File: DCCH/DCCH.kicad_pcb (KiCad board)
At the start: 4 copper layers, 127 x 76.2 mm, 57 parts, among them J1 Conn_01x02, J2 Conn_01x02, J211 Conn_01x02, J212 Conn_01x02, J221 Conn_01x02, J222 Conn_01x02, J231 Conn_01x02, J232 Conn_01x02, J241 Conn_01x02, J242 Conn_01x02, J3 Conn_02x04_Odd_Even, J4 Conn_02x04_Odd_Even, U11 SN74HC595, U12 SN74HC595, U13 SN74HC595, U14 SN74HC595, U21 SN754410, U22 SN754410, U23 SN754410, U24 SN754410

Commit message: Changed orientation again.
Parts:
- moved J3 102.4 mm to (71.8, 72.4), turned to 0 degrees
- moved D2 76.4 mm to (141.3, 105.4), turned to 180 degrees
- moved R2 74.1 mm to (137.2, 105.4), turned to 180 degrees
- moved J1 64.8 mm to (113.7, 110.5), turned to 0 degrees
- moved J2 61.4 mm to (137.2, 110.5), turned to 0 degrees
- moved D1 49.7 mm to (117.8, 105.4), turned to 180 degrees
- moved R1 48.6 mm to (113.6, 105.4), turned to 180 degrees
- moved C211 41.0 mm to (102.9, 47.3)
- moved C221 41.0 mm to (123.2, 47.3)
- moved C231 41.0 mm to (143.5, 47.3)
- moved C241 41.0 mm to (163.8, 47.3)
- moved U21 41.0 mm to (92.7, 46.4)
- moved U22 41.0 mm to (113.0, 46.4)
- moved U23 41.0 mm to (133.3, 46.4)
- moved U24 41.0 mm to (153.7, 46.4)
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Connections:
- J4 pad 1: SER-14 -> GND
- J4 pad 2: GND -> SER-14
- J4 pad 3: SYNC -> GND
- J4 pad 4: GND -> SYNC
- J4 pad 5: WRITE -> GND
- J4 pad 6: GND -> WRITE
- J4 pad 7: CLEAR -> GND
- J4 pad 8: GND -> CLEAR
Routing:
- net CLEAR: track 207.6 -> 291.6 mm
- net WRITE: track 205.0 -> 285.1 mm
- net SYNC: track 202.0 -> 277.7 mm
- net CON-12G: track 25.1 -> 53.8 mm
- net CON-14G: track 25.1 -> 53.8 mm
- net CON-13G: track 25.1 -> 53.8 mm
- net CON-11G: track 25.1 -> 53.8 mm
- net CON-14E: track 47.6 -> 30.7 mm
- net CON-13E: track 47.6 -> 30.7 mm
- net CON-11E: track 47.6 -> 30.7 mm
- net CON-12E: track 47.6 -> 30.7 mm
- net CON-13D: track 46.6 -> 29.7 mm
- net CON-11D: track 46.6 -> 29.7 mm
- net CON-14D: track 46.6 -> 29.7 mm
- net CON-12D: track 46.6 -> 29.7 mm
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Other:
- rule trace_min: 0.249999 -> 0.249936
- board text added: "+24V ON"
- board text added: "+5V ON"
- board text added: "5"
- board text added: "6"
- board text added: "7"
- board text added: "8"
- board text added: "GND"
- board text removed: "+24V DC"
- board text removed: "+5V DC"
- board text removed: "A"
- board text removed: "H"
- board text removed: "Power LEDs"

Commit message: Updated silksceen as well as plots.
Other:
- board text added: "IN"
- board text added: "OUT"
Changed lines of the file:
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@@
   (general
     (thickness 1.6)
-    (drawings 78)
+    (drawings 80)
     (tracks 496)
     (zones 0)
@@
     )
   )
+  (gr_text OUT (at 180.848 82.296) (layer F.SilkS)
+    (effects (font (size 0.889 0.889) (thickness 0.1524)))
+  )
+  (gr_text IN (at 73.152 82.296) (layer F.SilkS)
+    (effects (font (size 0.889 0.889) (thickness 0.1524)))
+  )
   (gr_text 8 (at 160.02 68.58) (layer F.SilkS)
     (effects (font (size 0.889 0.889) (thickness 0.1524)))
@@
   (gr_line (start 102.235 69.85) (end 102.235 78.74) (layer F.SilkS) (width 0.12))
   (gr_line (start 91.44 69.85) (end 102.235 69.85) (layer F.SilkS) (width 0.12))
-  (gr_text "+5V ON" (at 138.684 103.505) (layer F.SilkS)
+  (gr_text "+5V ON" (at 115.316 103.632) (layer F.SilkS)
     (effects (font (size 0.889 0.889) (thickness 0.1524)))
   )
-  (gr_text "+24V ON" (at 114.935 103.505) (layer F.SilkS)
+  (gr_text "+24V ON" (at 138.684 103.505) (layer F.SilkS)
     (effects (font (size 0.889 0.889) (thickness 0.1524)))
   )

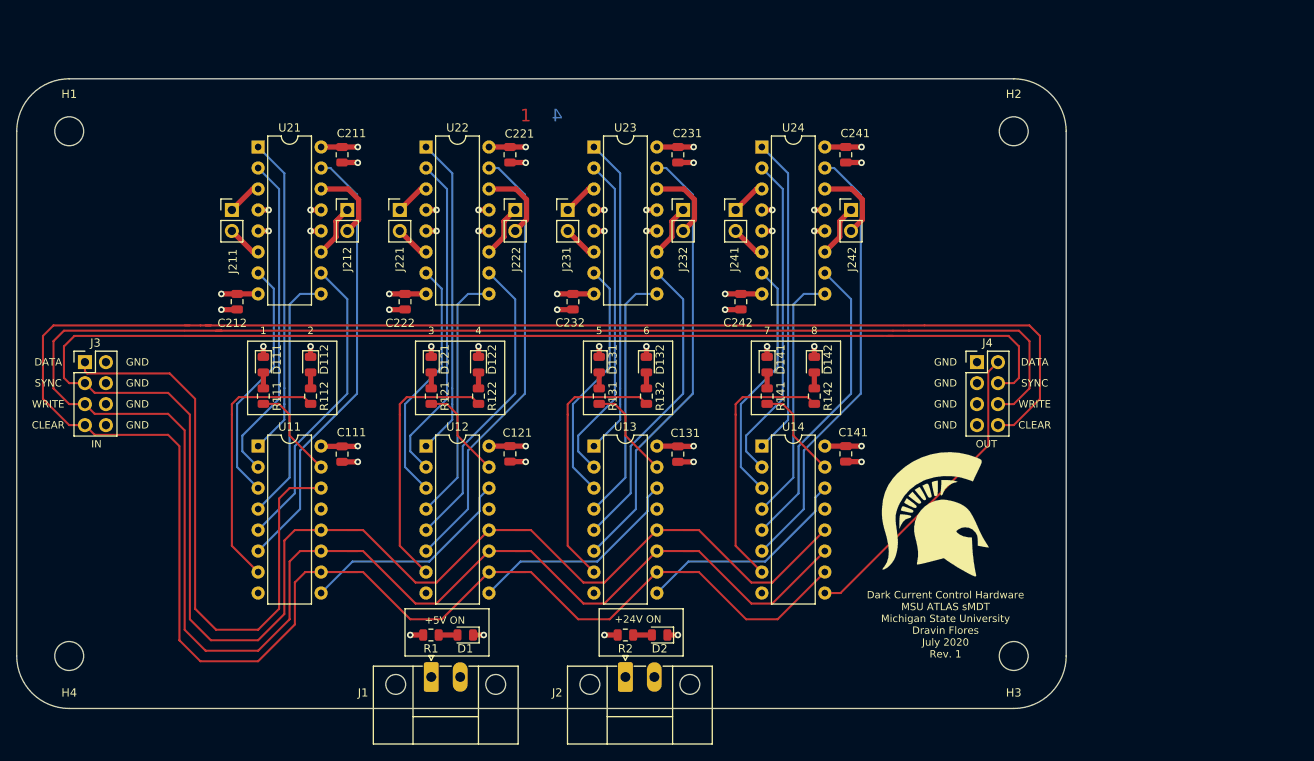
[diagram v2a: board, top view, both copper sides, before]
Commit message: Dean completely overhauled the board. Updated board and schematics
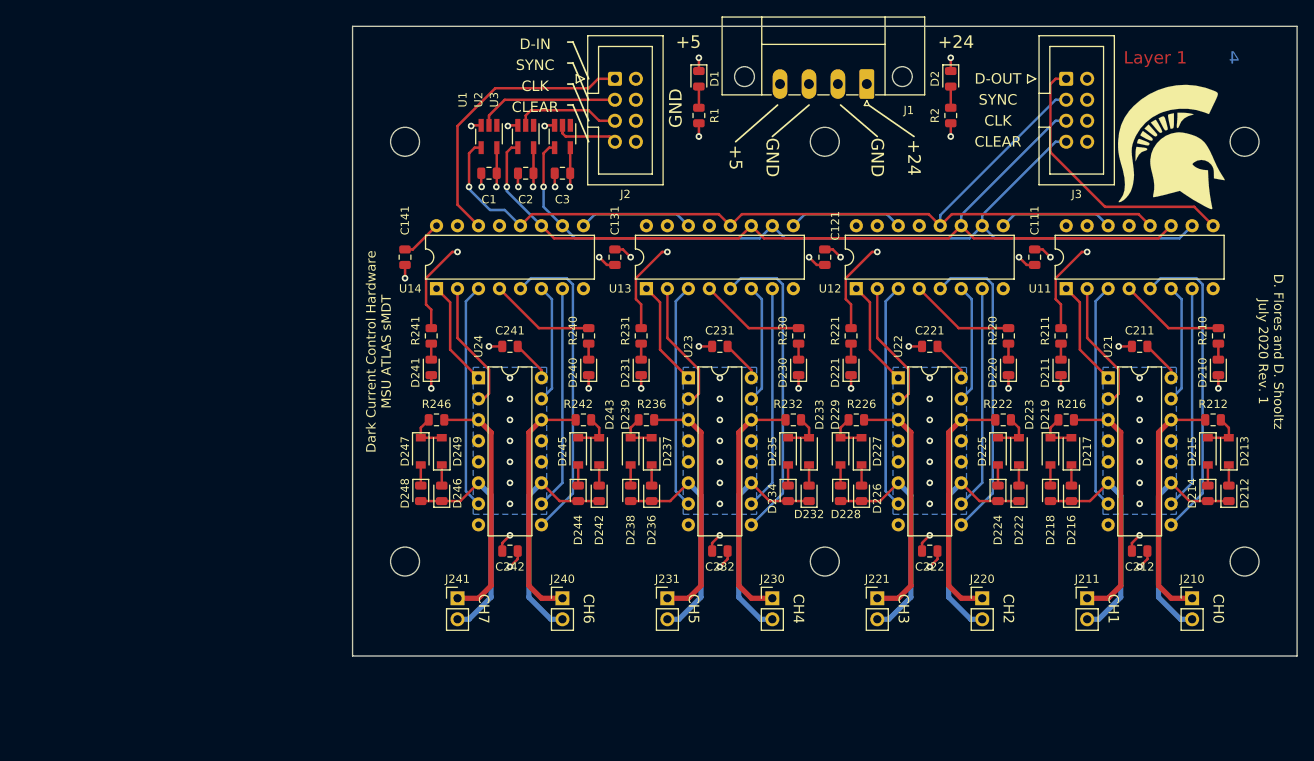
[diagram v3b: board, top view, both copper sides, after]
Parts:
- removed D111, D112, D121, D122, D131, D132, D141, D142: LED, LED_SMD:LED_0805_2012Metric
- removed J212, J222, J232, J242: Conn_01x02, Connector_PinHeader_2.54mm:PinHeader_1x02_P2.54mm_Vertical
- removed J4: Conn_02x04_Odd_Even, Connector_PinHeader_2.54mm:PinHeader_2x04_P2.54mm_Vertical
- removed R111, R112, R121, R122, R131, R132, R141, R142: R_US, Resistor_SMD:R_0805_2012Metric
- added C1: 0.1 uF, Capacitor_SMD:C_0805_2012Metric, F.Cu at (120.7, 49.5)
- added C2: 0.1 uF, Capacitor_SMD:C_0805_2012Metric, F.Cu at (125.1, 49.5)
- added C3: 0.1 uF, Capacitor_SMD:C_0805_2012Metric, F.Cu at (129.5, 49.5)
- added D210: LED, LED_SMD:LED_0805_2012Metric, F.Cu at (208.9, 73.0)
- added D211: LED, LED_SMD:LED_0805_2012Metric, F.Cu at (189.9, 73.0)
- added D212: GRN, LED_SMD:LED_0805_2012Metric, F.Cu at (210.2, 88.3)
- added D213: 1N4148W, Diode_SMD:D_SOD-123, F.Cu at (210.2, 83.2)
- added D214: RED, LED_SMD:LED_0805_2012Metric, F.Cu at (207.6, 88.3)
- added D215: 1N4148W, Diode_SMD:D_SOD-123, F.Cu at (207.6, 83.2)
- added D216: GRN, LED_SMD:LED_0805_2012Metric, F.Cu at (191.1, 88.3)
- added D217: 1N4148W, Diode_SMD:D_SOD-123, F.Cu at (191.1, 83.2)
- added D218: RED, LED_SMD:LED_0805_2012Metric, F.Cu at (188.6, 88.3)
- added D219: 1N4148W, Diode_SMD:D_SOD-123, F.Cu at (188.6, 83.2)
- added D220: LED, LED_SMD:LED_0805_2012Metric, F.Cu at (183.5, 73.0)
- added D221: RED, LED_SMD:LED_0805_2012Metric, F.Cu at (164.5, 73.0)
- added D222: GRN, LED_SMD:LED_0805_2012Metric, F.Cu at (184.8, 88.3)
- added D223: 1N4148W, Diode_SMD:D_SOD-123, F.Cu at (184.8, 83.2)
- added D224: RED, LED_SMD:LED_0805_2012Metric, F.Cu at (182.2, 88.3)
- added D225: 1N4148W, Diode_SMD:D_SOD-123, F.Cu at (182.2, 83.2)
- added D226: GRN, LED_SMD:LED_0805_2012Metric, F.Cu at (165.7, 88.3)
- added D227: 1N4148W, Diode_SMD:D_SOD-123, F.Cu at (165.7, 83.2)
- added D228: RED, LED_SMD:LED_0805_2012Metric, F.Cu at (163.2, 88.3)
- added D229: 1N4148W, Diode_SMD:D_SOD-123, F.Cu at (163.2, 83.2)
- added D230: RED, LED_SMD:LED_0805_2012Metric, F.Cu at (158.1, 73.0)
- added D231: RED, LED_SMD:LED_0805_2012Metric, F.Cu at (139.1, 73.0)
- added D232: GRN, LED_SMD:LED_0805_2012Metric, F.Cu at (159.4, 88.3)
- added D233: 1N4148W, Diode_SMD:D_SOD-123, F.Cu at (159.4, 83.2)
- added D234: RED, LED_SMD:LED_0805_2012Metric, F.Cu at (156.8, 88.3)
- added D235: 1N4148W, Diode_SMD:D_SOD-123, F.Cu at (156.8, 83.2)
- added D236: GRN, LED_SMD:LED_0805_2012Metric, F.Cu at (140.3, 88.3)
- added D237: 1N4148W, Diode_SMD:D_SOD-123, F.Cu at (140.3, 83.2)
- added D238: RED, LED_SMD:LED_0805_2012Metric, F.Cu at (137.8, 88.3)
- added D239: 1N4148W, Diode_SMD:D_SOD-123, F.Cu at (137.8, 83.2)
- added D240: RED, LED_SMD:LED_0805_2012Metric, F.Cu at (132.7, 73.0)
- added D241: RED, LED_SMD:LED_0805_2012Metric, F.Cu at (113.7, 73.0)
- added D242: GRN, LED_SMD:LED_0805_2012Metric, F.Cu at (134.0, 88.3)
- added D243: 1N4148W, Diode_SMD:D_SOD-123, F.Cu at (134.0, 83.2)
- added D244: RED, LED_SMD:LED_0805_2012Metric, F.Cu at (131.4, 88.3)
- added D245: 1N4148W, Diode_SMD:D_SOD-123, F.Cu at (131.4, 83.2)
- added D246: GRN, LED_SMD:LED_0805_2012Metric, F.Cu at (114.9, 88.3)
- added D247: 1N4148W, Diode_SMD:D_SOD-123, F.Cu at (114.9, 83.2)
- added D248: RED, LED_SMD:LED_0805_2012Metric, F.Cu at (112.4, 88.3)
- added D249: 1N4148W, Diode_SMD:D_SOD-123, F.Cu at (112.4, 83.2)
- added H5: MountingHole, MountingHole:MountingHole_3.5mm, F.Cu at (161.3, 45.7)
- added H6: MountingHole, MountingHole:MountingHole_3.5mm, F.Cu at (161.3, 96.5)
- added J210: Conn_01x02, Connector_PinHeader_2.54mm:PinHeader_1x02_P2.54mm_Vertical, F.Cu at (205.7, 101.0)
- added J220: Conn_01x02, Connector_PinHeader_2.54mm:PinHeader_1x02_P2.54mm_Vertical, F.Cu at (180.3, 101.0)
- added J230: Conn_01x02, Connector_PinHeader_2.54mm:PinHeader_1x02_P2.54mm_Vertical, F.Cu at (154.9, 101.0)
- added J240: Conn_01x02, Connector_PinHeader_2.54mm:PinHeader_1x02_P2.54mm_Vertical, F.Cu at (129.5, 101.0)
- added R210: 270, Resistor_SMD:R_0805_2012Metric, F.Cu at (208.9, 69.2)
- added R211: 270, Resistor_SMD:R_0805_2012Metric, F.Cu at (189.9, 69.2)
- added R212: 2k, Resistor_SMD:R_0805_2012Metric, F.Cu at (208.3, 79.4)
- added R216: 2k, Resistor_SMD:R_0805_2012Metric, F.Cu at (190.5, 79.4)
- added R220: 270, Resistor_SMD:R_0805_2012Metric, F.Cu at (183.5, 69.2)
- added R221: 270, Resistor_SMD:R_0805_2012Metric, F.Cu at (164.5, 69.2)
- added R222: 2k, Resistor_SMD:R_0805_2012Metric, F.Cu at (182.9, 79.4)
- added R226: 2k, Resistor_SMD:R_0805_2012Metric, F.Cu at (165.1, 79.4)
- added R230: 270, Resistor_SMD:R_0805_2012Metric, F.Cu at (158.1, 69.2)
- added R231: 270, Resistor_SMD:R_0805_2012Metric, F.Cu at (139.1, 69.2)
- added R232: 2k, Resistor_SMD:R_0805_2012Metric, F.Cu at (157.5, 79.4)
- added R236: 2k, Resistor_SMD:R_0805_2012Metric, F.Cu at (139.7, 79.4)
- added R240: 270, Resistor_SMD:R_0805_2012Metric, F.Cu at (132.7, 69.2)
- added R241: 270, Resistor_SMD:R_0805_2012Metric, F.Cu at (113.7, 69.2)
- added R242: 2k, Resistor_SMD:R_0805_2012Metric, F.Cu at (132.1, 79.4)
- added R246: 2k, Resistor_SMD:R_0805_2012Metric, F.Cu at (114.3, 79.4)
- added U1: 74LVC1G17, Package_TO_SOT_SMD:SOT-23-5_HandSoldering, F.Cu at (120.7, 45.1)
- added U2: 74LVC1G17, Package_TO_SOT_SMD:SOT-23-5_HandSoldering, F.Cu at (125.1, 45.1)
- added U3: 74LVC1G17, Package_TO_SOT_SMD:SOT-23-5_HandSoldering, F.Cu at (129.5, 45.1)
- J1: value Conn_01x02 -> Conn_01x04; footprint Connector_Phoenix_MC:PhoenixContact_MC_1,5_2-GF-3.5_1x02_P3.50mm_Horizontal_ThreadedFlange_MountHole -> Connector_Phoenix_MC:PhoenixContact_MC_1,5_4-GF-3.5_1x04_P3.50mm_Horizontal_ThreadedFlange_MountHole
- J2: value Conn_01x02 -> Conn_02x04_Odd_Even; footprint Connector_Phoenix_MC:PhoenixContact_MC_1,5_2-GF-3.5_1x02_P3.50mm_Horizontal_ThreadedFlange_MountHole -> Connector_IDC:IDC-Header_2x04_P2.54mm_Vertical
- J3: footprint Connector_PinHeader_2.54mm:PinHeader_2x04_P2.54mm_Vertical -> Connector_IDC:IDC-Header_2x04_P2.54mm_Vertical
- R1: value R_US -> 270
- R2: value R_US -> 2k
- moved H4 142.7 mm to (212.1, 96.5)
- moved J3 123.6 mm to (190.5, 38.1)
- moved J211 113.7 mm to (193.0, 101.0)
- moved C212 113.3 mm to (199.4, 95.2), turned to 0 degrees
- moved U21 106.6 mm to (195.6, 74.3)
- moved U11 99.6 mm to (190.5, 63.5), turned to 90 degrees
- moved C211 99.3 mm to (199.4, 70.5), turned to 180 degrees
- moved J1 89.0 mm to (166.4, 38.7), turned to 180 degrees
- moved C111 87.1 mm to (186.7, 59.7)
- moved D2 76.0 mm to (176.5, 38.1), turned to 270 degrees
- moved H3 74.5 mm to (110.5, 96.5)
- moved J221 74.5 mm to (167.6, 101.0)
- moved R2 74.2 mm to (176.5, 42.5), turned to 270 degrees
- moved D1 73.0 mm to (146.1, 38.1), turned to 270 degrees
- moved J2 72.4 mm to (135.9, 38.1)
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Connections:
- net CLEAR renamed CLEARbuf
- net CON-11B renamed Bit-6
- net CON-11C renamed Bit-5
- net CON-11D renamed Bit-4
- net CON-11G renamed Bit-1
- net CON-12B renamed Bit-14
- net CON-12C renamed Bit-13
- net CON-12D renamed Bit-12
- net CON-12G renamed Bit-9
- net CON-13B renamed Bit-22
- net CON-13C renamed Bit-21
- net CON-13D renamed Bit-20
- net CON-13G renamed Bit-17
- net CON-14B renamed Bit-30
- net CON-14C renamed Bit-29
- net CON-14D renamed Bit-28
- net CON-14G renamed Bit-25
- net OUT-1A renamed Net-(J211-Pad1)
- net OUT-1B renamed Net-(D216-Pad1)
- net OUT-3A renamed Net-(J221-Pad1)
- net OUT-3B renamed Net-(D226-Pad1)
- net OUT-5A renamed Net-(J231-Pad1)
- net OUT-5B renamed Net-(D236-Pad1)
- net OUT-7A renamed Net-(J241-Pad1)
- net OUT-7B renamed Net-(D246-Pad1)
- net SYNC renamed SYNCbuf
- net WRITE renamed CLKbuf
- J1 pad 1: +5V -> +24V
- J2 pad 1: +24V -> Net-(J2-Pad1)
- J3 pad 1: DATA-IN -> Net-(J3-Pad1)
- U11 pad 14: DATA-IN -> Net-(U11-Pad14)
- U11 pad 15: CON-11A -> Bit-7
- U11 pad 4: CON-11E -> Bit-3
- U11 pad 5: CON-11F -> Bit-2
- U11 pad 7: CON-11H -> Bit-0
- U11 pad 9: SER-11 -> Net-(J3-Pad1)
- U12 pad 14: SER-11 -> Net-(U12-Pad14)
- U12 pad 15: CON-12A -> Bit-15
- U12 pad 4: CON-12E -> Bit-11
- U12 pad 5: CON-12F -> Bit-10
- U12 pad 7: CON-12H -> Bit-8
- U12 pad 9: SER-12 -> Net-(U11-Pad14)
- U13 pad 14: SER-12 -> Net-(U13-Pad14)
- U13 pad 15: CON-13A -> Bit-23
- U13 pad 4: CON-13E -> Bit-19
- U13 pad 5: CON-13F -> Bit-18
- U13 pad 7: CON-13H -> Bit-16
- U13 pad 9: SER-13 -> Net-(U12-Pad14)
- U14 pad 14: SER-13 -> Net-(J2-Pad1)
- U14 pad 15: CON-14A -> Bit-31
- U14 pad 4: CON-14E -> Bit-27
- U14 pad 5: CON-14F -> Bit-26
- U14 pad 7: CON-14H -> Bit-24
- U14 pad 9: SER-14 -> Net-(U13-Pad14)
- U21 pad 10: CON-11F -> Bit-0
- U21 pad 11: OUT-2A -> Net-(D212-Pad1)
- U21 pad 14: OUT-2B -> Net-(J210-Pad1)
- U21 pad 9: CON-11E -> Bit-2
- U22 pad 10: CON-12F -> Bit-8
- U22 pad 11: OUT-4A -> Net-(D222-Pad1)
- U22 pad 14: OUT-4B -> Net-(J220-Pad1)
- U22 pad 9: CON-12E -> Bit-10
- U23 pad 10: CON-13F -> Bit-16
- U23 pad 11: OUT-6A -> Net-(D232-Pad1)
- U23 pad 14: OUT-6B -> Net-(J230-Pad1)
- U23 pad 9: CON-13E -> Bit-18
- U24 pad 10: CON-14F -> Bit-24
- U24 pad 11: OUT-8A -> Net-(D242-Pad1)
- U24 pad 14: OUT-8B -> Net-(J240-Pad1)
- U24 pad 9: CON-14E -> Bit-26
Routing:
- net CLEARbuf: track 291.6 -> 106.4 mm, vias 0 -> 1
- net CLKbuf: track 285.1 -> 110.9 mm, vias 0 -> 1
- net SYNCbuf: track 277.7 -> 116.1 mm, vias 0 -> 1
- net DATA-IN: track 72.4 -> 0.00 mm
- net Bit-9: track 53.8 -> 14.4 mm
- net Bit-17: track 53.8 -> 14.4 mm
- net Bit-25: track 53.8 -> 14.4 mm
- net Bit-1: track 53.8 -> 14.4 mm
- net Bit-10: track 0.00 -> 37.9 mm
- net Bit-26: track 0.00 -> 37.9 mm
- net Bit-18: track 0.00 -> 37.9 mm
- net Bit-2: track 0.00 -> 37.9 mm
- net SER-14: track 37.7 -> 0.00 mm
- net CON-14F: track 36.9 -> 0.00 mm
- net CON-13F: track 36.9 -> 0.00 mm
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- added copper zone on B.Cu, net GND
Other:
- board size 127 x 76.2 mm -> 114.3 x 76.2 mm
- net class Default: clearance 0.2 -> 0.2794; trace_width 0.25 -> 0.3048
- rule trace_clearance: 0.2 -> 0.2794
- rule trace_min: 0.249936 -> 0.3048
- board text added: "+24"
- board text added: "+5"
- board text added: "CH0"
- board text added: "CH1"
- board text added: "CH2"
- board text added: "CH3"
- board text added: "CH4"
- board text added: "CH5"
- board text added: "CH6"
- board text added: "CH7"
- board text added: "CLK"
- board text added: "D-IN"
- board text added: "D-OUT"
- board text added: "D. Flores and D. Shooltz July 2020 Rev. 1"
- board text added: "Dark Current Control Hardware MSU ATLAS sMDT"
- board text added: "Layer 1"
- board text removed: "+24V ON"
- board text removed: "+5V ON"
- board text removed: "1"
- board text removed: "5"
- board text removed: "6"
- board text removed: "7"
- board text removed: "8"
- board text removed: "DATA"
- board text removed: "Dark Current Control Hardware MSU ATLAS sMDT Michigan State University Dravin Flores July 2020 Rev. 1"
- board text removed: "IN"
- board text removed: "LAYER"
- board text removed: "OUT"
- board text removed: "WRITE"

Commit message: Updated plots.
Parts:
- moved G*** 1.27 mm to (204.5, 46.4)
